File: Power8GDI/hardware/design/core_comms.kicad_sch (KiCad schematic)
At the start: 16 parts, among them U103 TCAN1042HGVDRQ1, U104 TLIN1029ADRQ1

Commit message: Checkpoint integrated 37-sheet schematic before Huge scope revision
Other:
- note added: "CAN1_H/L are vehicle-side nets. STB high by default; MCU PH2 pad43 enables low. DNP termination only after network topology review. EMC/ESD bench qualification pending. CAN2 and LIN2 use the comms2 sheet. PH2/PH3 GPIO additions are provisional schematic assignments."
- note removed: "CAN1_H/L are vehicle-side nets. STB high by default; MCU PH2 pad43 enables low. DNP termination only after network topology review. EMC/ESD bench qualification pending. CAN2 and LIN2 remain unassigned. PH2/PH3 GPIO additions are provisional schematic assignments."
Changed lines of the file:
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@@
 (wire (pts (xy 204.47 123.19) (xy 204.47 130.81)) (stroke (width 0) (type default)))
 (global_label "CAN1_L" (shape bidirectional) (at 204.47 130.81 90) (effects (font (size 1.016 1.016)) (justify right bottom)))
-(text "CAN1_H/L are vehicle-side nets. STB high by default; MCU PH2 pad43 enables low.\nDNP termination only after network topology review. EMC/ESD bench qualification pending.\nCAN2 and LIN2 remain unassigned. PH2/PH3 GPIO additions are provisional schematic assignments." (at 25.4 175 0) (effects (font (size 1.27 1.27)) (justify left top)))
+(text "CAN1_H/L are vehicle-side nets. STB high by default; MCU PH2 pad43 enables low.\nDNP termination only after network topology review. EMC/ESD bench qualification pending.\nCAN2 and LIN2 use the comms2 sheet. PH2/PH3 GPIO additions are provisional schematic assignments." (at 25.4 175 0) (effects (font (size 1.27 1.27)) (justify left top)))
 (symbol (lib_id "Power8GDI_Core:PESD2CAN") (at 245.11 129.54 0) (unit 1) (in_bom yes) (on_board yes) (dnp no) (property "Reference" "D101" (at 245.11 121.92 0) (effects (font (size 1.27 1.27)))) (property "Value" "PESD2CAN" (at 245.11 137.16 0) (effects (font (size 1.27 1.27)))) (property "Footprint" "Package_TO_SOT_SMD:SOT-23" (at 245.11 129.54 0) (effects (font (size 1.27 1.27)) (hide yes))) (property "Design note" "Nexperia Rev2 pinning1/2lines3common; close connector; ground surge return review" (at 245.11 129.54 0) (effects (font (size 1.27 1.27)) (hide yes))) (pin "1") (pin "2") (pin "3") (instances (project "Power8GDI_Core" (path "/f4d21065-0a5b-5086-a08e-1af9469f04bd/a46f09d2-745d-5ec9-9128-e45b02fcfc2a" (reference "D101") (unit 1)))))
 (wire (pts (xy 234.95 124.46) (xy 227.33 124.46)) (stroke (width 0) (type default)))

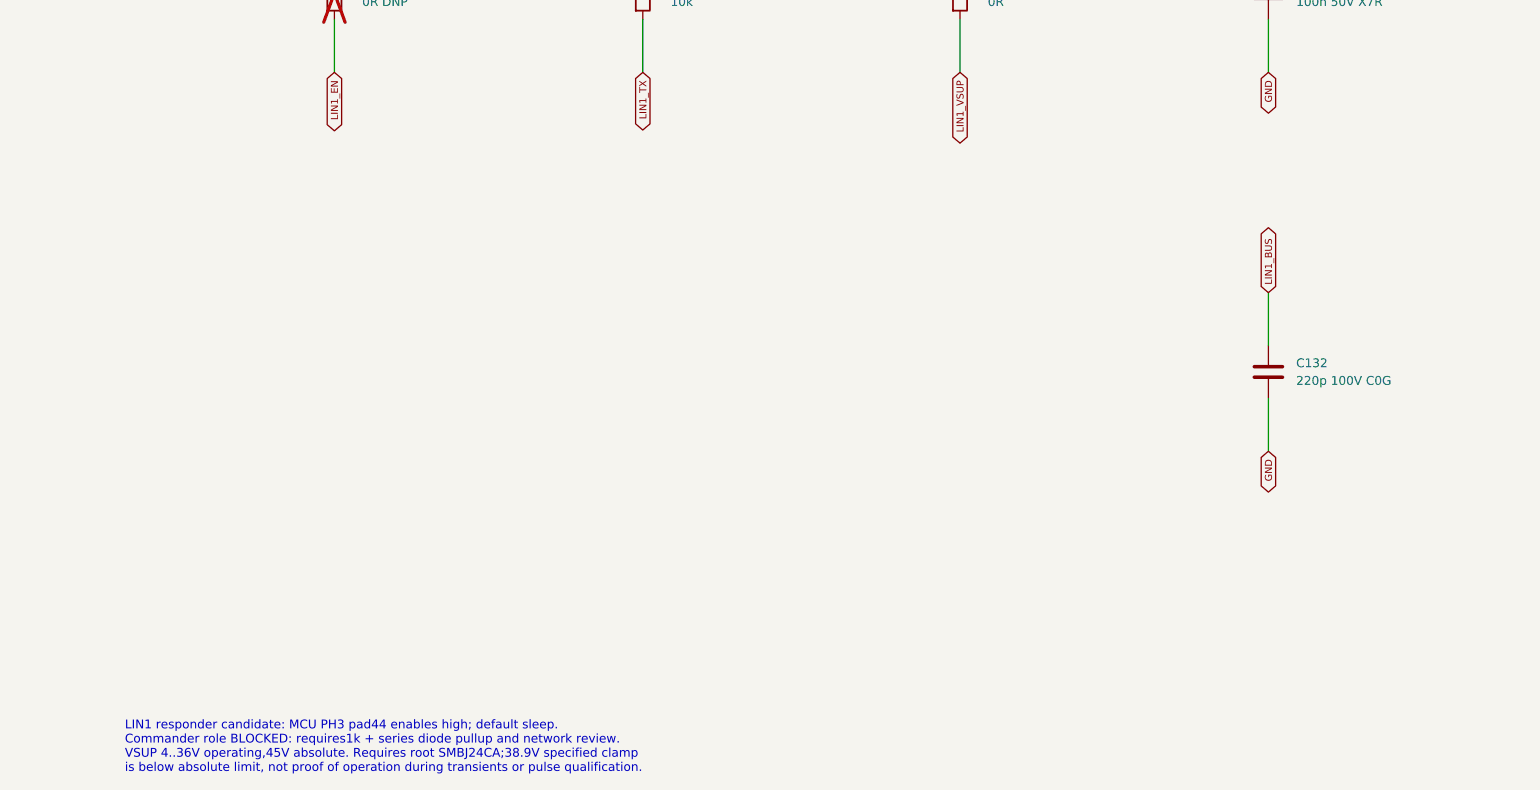
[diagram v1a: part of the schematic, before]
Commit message: Integrate protected GDI and CAN wideband nodes with Huge channel allocation
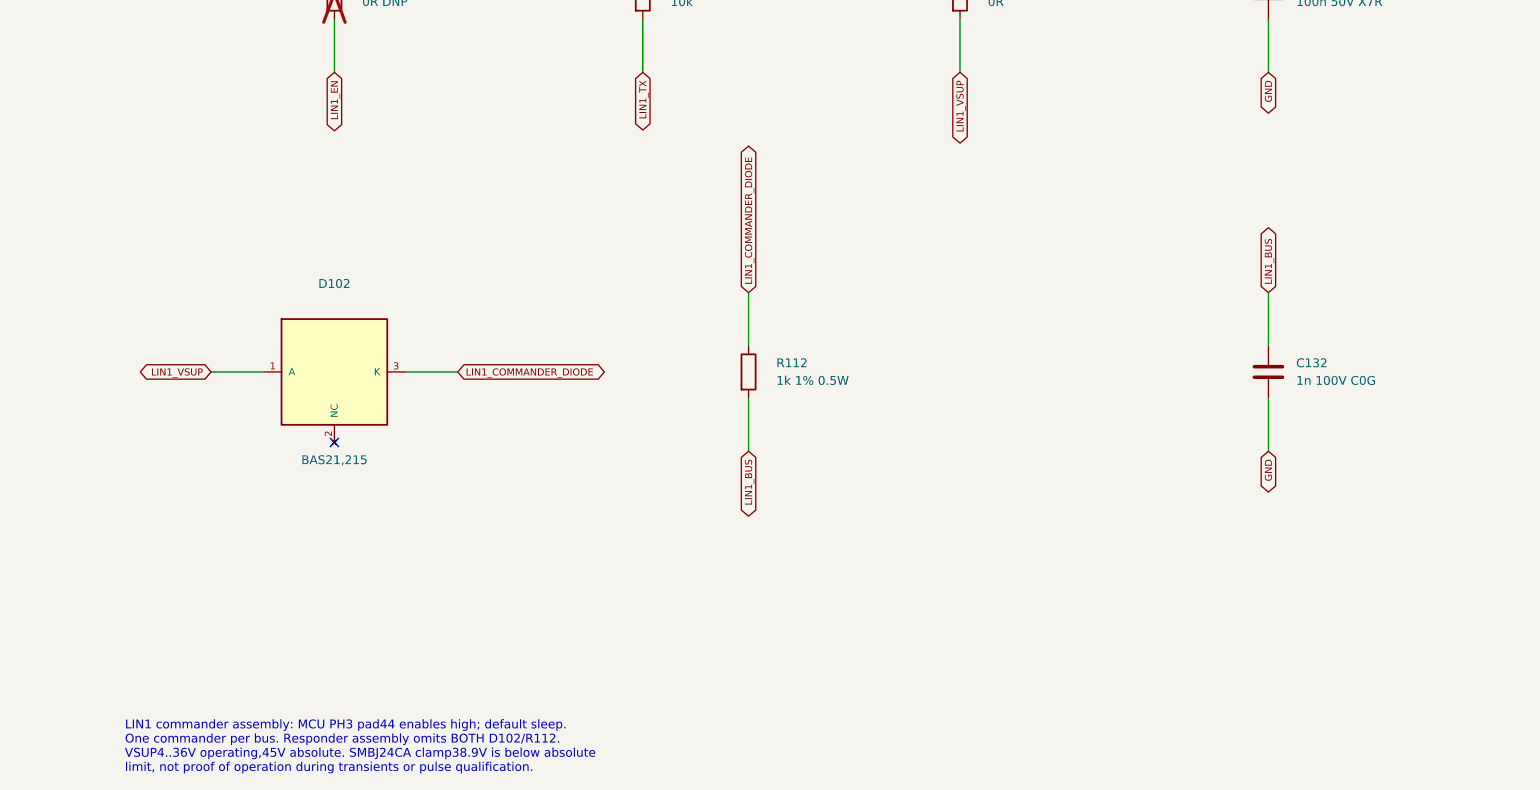
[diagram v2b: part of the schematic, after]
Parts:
- added D102: BAS21,215, Package_TO_SOT_SMD:SOT-23, symbol Power8GDI_Core:Core_BAS21
- added R112: 1k 1% 0.5W, Resistor_SMD:R_1206_3216Metric, symbol Power8GDI_Core:R
- C132: value 220p 100V C0G -> 1n 100V C0G; Design note Respondermode buscap TI Fig10-1; busEMC/loadbudget pending -> Commander bus capacitance; verify total cable/node capacita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
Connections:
- net LIN1_BUS: now also R112.2
- net LIN1_VSUP: now also D102.1 (A)
- new net LIN1_COMMANDER_DIODE: D102.3 (K), R112.1
- no-connect marks 2 -> 3
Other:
- note added: "LIN1 commander assembly: MCU PH3 pad44 enables high; default sleep. One commander per bus. Responder assembly omits BOTH D102/R112. VSUP4..36V operating,45V absolute. SMBJ24CA clamp38.9V is below absolute limit, not proof of operation during transients or pulse qualification."
- note removed: "LIN1 responder candidate: MCU PH3 pad44 enables high; default sleep. Commander role BLOCKED: requires1k + series diode pullup and network review. VSUP 4..36V operating,45V absolute. Requires root SMBJ24CA;38.9V specified clamp is below absolute limit, not proof of operation during transients or pulse qualification."
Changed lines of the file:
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@@
 (wire (pts (xy 510.54 168.91) (xy 510.54 176.53)) (stroke (width 0) (type default)))
 (global_label "GND" (shape bidirectional) (at 510.54 176.53 90) (effects (font (size 1.016 1.016)) (justify right bottom)))
-(symbol (lib_id "Power8GDI_Core:C") (at 464.82 219.71 0) (unit 1) (in_bom yes) (on_board yes) (dnp no) (property "Reference" "C132" (at 468.82 218.44 0) (effects (font (size 1.27 1.27)) (justify left))) (property "Value" "220p 100V C0G" (at 468.82 220.98 0) (effects (font (size 1.27 1.27)) (justify left))) (property "Footprint" "Capacitor_SMD:C_0603_1608Metric" (at 464.82 219.71 0) (effects (font (size 1.27 1.27)) (hide yes))) (property "Design note" "Respondermode buscap TI Fig10-1; busEMC/loadbudget pending" (at 464.82 219.71 0) (effects (font (size 1.27 1.27)) (hide yes))) (pin "1") (pin "2") (instances (project "Power8GDI_Core" (path "/f4d21065-0a5b-5086-a08e-1af9469f04bd/a46f09d2-745d-5ec9-9128-e45b02fcfc2a" (reference "C132") (unit 1)))))
+(symbol (lib_id "Power8GDI_Core:C") (at 464.82 219.71 0) (unit 1) (in_bom yes) (on_board yes) (dnp no) (property "Reference" "C132" (at 468.82 218.44 0) (effects (font (size 1.27 1.27)) (justify left))) (property "Value" "1n 100V C0G" (at 468.82 220.98 0) (effects (font (size 1.27 1.27)) (justify left))) (property "Footprint" "Capacitor_SMD:C_0603_1608Metric" (at 464.82 219.71 0) (effects (font (size 1.27 1.27)) (hide yes))) (property "Design note" "Commander bus capacitance; verify total cable/node capacitance" (at 464.82 219.71 0) (effects (font (size 1.27 1.27)) (hide yes))) (pin "1") (pin "2") (instances (project "Power8GDI_Core" (path "/f4d21065-0a5b-5086-a08e-1af9469f04bd/a46f09d2-745d-5ec9-9128-e45b02fcfc2a" (reference "C132") (unit 1)))))
 (wire (pts (xy 464.82 215.9) (xy 464.82 208.28)) (stroke (width 0) (type default)))
 (global_label "LIN1_BUS" (shape bidirectional) (at 464.82 208.28 270) (effects (font (size 1.016 1.016)) (justify left bottom)))
 (wire (pts (xy 464.82 223.52) (xy 464.82 231.14)) (stroke (width 0) (type default)))
 (global_label "GND" (shape bidirectional) (at 464.82 231.14 90) (effects (font (size 1.016 1.016)) (justify right bottom)))
-(text "LIN1 responder candidate: MCU PH3 pad44 enables high; default sleep.\nCommander role BLOCKED: requires1k + series diode pullup and network review.\nVSUP 4..36V operating,45V absolute. Requires root SMBJ24CA;38.9V specified clamp\nis below absolute limit, not proof of operation during transients or pulse qualification." (at 300 270 0) (effects (font (size 1.27 1.27)) (justify left top)))
+(symbol (lib_id "Power8GDI_Core:Core_BAS21") (at 330.2 219.71 0) (unit 1) (in_bom yes) (on_board yes) (dnp no) (property "Reference" "D102" (at 330.2 207.01 0) (effects (font (size 1.27 1.27)))) (property "Value" "BAS21,215" (at 330.2 232.41 0) (effects (font (size 1.27 1.27)))) (property "Footprint" "Package_TO_SOT_SMD:SOT-23" (at 330.2 219.71 0) (effects (font (size 1.27 1.27)) (hide yes))) (property "Design note" "Commander assembly; remove D102 and R112 for responder-only topology" (at 330.2 219.71 0) (effects (font (size 1.27 1.27)) (hide yes))) (pin "1") (pin "3") (pin "2") (instances (project "Power8GDI_Core" (path "/f4d21065-0a5b-5086-a08e-1af9469f04bd/a46f09d2-745d-5ec9-9128-e45b02fcfc2a" (reference "D102") (unit 1)))))
+(wire (pts (xy 320.04 219.71) (xy 312.42 219.71)) (stroke (width 0) (type default)))
+(global_label "LIN1_VSUP" (shape bidirectional) (at 312.42 219.71 0) (effects (font (size 1.016 1.016)) (justify right bottom)))
+(wire (pts (xy 340.36 219.71) (xy 347.98 219.71)) (stroke (width 0) (type default)))
+(global_label "LIN1_COMMANDER_DIODE" (shape bidirectional) (at 347.98 219.71 180) (effects (font (size 1.016 1.016)) (justify left bottom)))
+(no_connect (at 330.2 229.87))
+(symbol (lib_id "Power8GDI_Core:R") (at 389.89 219.71 0) (unit 1) (in_bom yes) (on_board yes) (dnp no) (property "Reference" "R112" (at 393.89 218.44 0) (effects (font (size 1.27 1.27)) (justify left))) (property "Value" "1k 1% 0.5W" (at 393.89 220.98 0) (effects (font (size 1.27 1.27)) (justify left))) (property "Footprint" "Resistor_SMD:R_1206_3216Metric" (at 389.89 219.71 0) (effects (font (size 1.27 1.27)) (hide yes))) (property "Design note" "16V dominant bound0.256W; pulse/voltage derating must be checked" (at 389.89 219.71 0) (effects (font (size 1.27 1.27)) (hide yes))) (pin "1") (pin "2") (instances (project "Power8GDI_Core" (path "/f4d21065-0a5b-5086-a08e-1af9469f04bd/a46f09d2-745d-5ec9-9128-e45b02fcfc2a" (reference "R112") (unit 1)))))
+(wire (pts (xy 389.89 215.9) (xy 389.89 208.28)) (stroke (width 0) (type default)))
+(global_label "LIN1_COMMANDER_DIODE" (shape bidirectional) (at 389.89 208.28 270) (effects (font (size 1.016 1.016)) (justify left bottom)))
+(wire (pts (xy 389.89 223.52) (xy 389.89 231.14)) (stroke (width 0) (type default)))
+(global_label "LIN1_BUS" (shape bidirectional) (at 389.89 231.14 90) (effects (font (size 1.016 1.016)) (justify right bottom)))
+(text "LIN1 commander assembly: MCU PH3 pad44 enables high; default sleep.\nOne commander per bus. Responder assembly omits BOTH D102/R112.\nVSUP4..36V operating,45V absolute. SMBJ24CA clamp38.9V is below absolute\nlimit, not proof of operation during transients or pulse qualification." (at 300 270 0) (effects (font (size 1.27 1.27)) (justify left top)))
 (sheet_instances (path "/" (page "1"))))

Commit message: Review B58 injector power stage and bind selected GDI6 BOM
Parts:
- C127, C128, C130: Hardware_Qualification (none) -> BOARD_QUALIFICATION_PENDING; MPN (none) -> C0603C104K5RACTU; Manufacturer (none) -> KEMET; Procurement_Status (none) -> SELECTED_CATALOG_ITEM; Purchase_Released (none) -> false; Selection_Gaps (none) -> []; Selection_ID (none) -> SEL-6bf9727c4e40; Selection_Ratings (none) -> {"capacitance_pf": 100000, "dielectric": "X7R", "rated_volt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; Selection_Source_URLs (none) -> https://search.kemet.com/download/specsheet/C0603C104K5RACTU
- C131: Hardware_Qualification (none) -> BOARD_QUALIFICATION_PENDING; MPN (none) -> C0805C105K5RACTU; Manufacturer (none) -> KEMET; Procurement_Status (none) -> SELECTED_CATALOG_ITEM; Purchase_Released (none) -> false; Selection_Gaps (none) -> []; Selection_ID (none) -> SEL-838906dbfe60; Selection_Ratings (none) -> {"capacitance_pf": 1000000, "dc_bias_qualification": "PENDI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; Selection_Source_URLs (none) -> https://search.kemet.com/component-documentation/download/s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
- C132: Hardware_Qualification (none) -> BOARD_QUALIFICATION_PENDING; MPN (none) -> C0603C102J1GACTU; Manufacturer (none) -> KEMET; Procurement_Status (none) -> SELECTED_CATALOG_ITEM; Purchase_Released (none) -> false; Selection_Gaps (none) -> []; Selection_ID (none) -> SEL-ec742f39ec1f; Selection_Ratings (none) -> {"capacitance_pf": 1000, "dielectric": "C0G", "rated_voltag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; Selection_Source_URLs (none) -> https://search.kemet.com/download/specsheet/C0603C102J1GACTU
- D101: Hardware_Qualification (none) -> PINOUT_RATINGS_AND_DELIVERY_SUFFIX_REVIEW_PENDING; MPN (none) -> PESD2CAN,215; Manufacturer (none) -> Nexperia; Procurement_Status (none) -> REFERENCE_MPN_RETAINED; Purchase_Released (none) -> false; Selection_Gaps (none) -> ["Existing schematic MPN retained. Complete circuit rating/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; Selection_ID (none) -> SEL-397878b612f9; Selection_Ratings (none) -> {}; Selection_Source_URLs (none) -> https://www.nexperia.com/product/PESD2CAN
- D102: Hardware_Qualification (none) -> PINOUT_RATINGS_AND_DELIVERY_SUFFIX_REVIEW_PENDING; MPN (none) -> BAS21,215; Manufacturer (none) -> Nexperia; Procurement_Status (none) -> REFERENCE_MPN_RETAINED; Purchase_Released (none) -> false; Selection_Gaps (none) -> ["Existing schematic MPN retained. Complete circuit rating/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; Selection_ID (none) -> SEL-3ac3f96db10b; Selection_Ratings (none) -> {}; Selection_Source_URLs (none) -> https://www.nexperia.com/product/BAS21
- R104, R108, R110: Hardware_Qualification (none) -> BOARD_QUALIFICATION_PENDING; MPN (none) -> CRCW060310K0FKEA; Manufacturer (none) -> Vishay; Procurement_Status (none) -> SELECTED_FAMILY_CODE; Purchase_Released (none) -> false; Selection_Gaps (none) -> []; Selection_ID (none) -> SEL-9c0806476875; Selection_Ratings (none) -> {"aec_q200": true, "derating": "Use manufacturer power vers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; Selection_Source_URLs (none) -> https://www.vishay.com/docs/20035/dcrcwe3.pdf
- R107: Hardware_Qualification (none) -> BOARD_QUALIFICATION_PENDING; MPN (none) -> CRCW06034K70FKEA; Manufacturer (none) -> Vishay; Procurement_Status (none) -> SELECTED_FAMILY_CODE; Purchase_Released (none) -> false; Selection_Gaps (none) -> []; Selection_ID (none) -> SEL-1f010ac9622d; Selection_Ratings (none) -> {"aec_q200": true, "derating": "Use manufacturer power vers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; Selection_Source_URLs (none) -> https://www.vishay.com/docs/20035/dcrcwe3.pdf
- R111: Hardware_Qualification (none) -> BOARD_QUALIFICATION_PENDING; MPN (none) -> CRCW06030000Z0EA; Manufacturer (none) -> Vishay; Procurement_Status (none) -> SELECTED_FAMILY_CODE; Purchase_Released (none) -> false; Selection_Gaps (none) -> []; Selection_ID (none) -> SEL-8473f02313b2; Selection_Ratings (none) -> {"aec_q200": true, "current_a": 2, "power_reference_tempera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; Selection_Source_URLs (none) -> https://www.vishay.com/docs/20035/dcrcwe3.pdf
- R112: Hardware_Qualification (none) -> BOARD_QUALIFICATION_PENDING; MPN (none) -> CRCW12061K00FKEAHP; Manufacturer (none) -> Vishay; Procurement_Status (none) -> SELECTED_CATALOG_ITEM; Purchase_Released (none) -> false; Selection_Gaps (none) -> []; Selection_ID (none) -> SEL-515f600e0ec3; Selection_Ratings (none) -> {"aec_q200": true, "derating": "Use manufacturer power vers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; Selection_Source_URLs (none) -> https://www.vishay.com/docs/20043/crcwhpe3.pdf https://www.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
- U103: Hardware_Qualification (none) -> PINOUT_RATINGS_AND_DELIVERY_SUFFIX_REVIEW_PENDING; MPN (none) -> TCAN1042HGVDRQ1; Manufacturer (none) -> Texas Instruments; Procurement_Status (none) -> REFERENCE_MPN_RETAINED; Purchase_Released (none) -> false; Selection_Gaps (none) -> ["Existing schematic MPN retained. Complete circuit rating/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; Selection_ID (none) -> SEL-c86778911c36; Selection_Ratings (none) -> {}; Selection_Source_URLs (none) -> https://www.ti.com/product/TCAN1042H-Q1/part-details/TCAN10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
- U104: Hardware_Qualification (none) -> PINOUT_RATINGS_AND_DELIVERY_SUFFIX_REVIEW_PENDING; MPN (none) -> TLIN1029ADRQ1; Manufacturer (none) -> Texas Instruments; Procurement_Status (none) -> REFERENCE_MPN_RETAINED; Purchase_Released (none) -> false; Selection_Gaps (none) -> ["Existing schematic MPN retained. Complete circuit rating/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; Selection_ID (none) -> SEL-d38cf124d61a; Selection_Ratings (none) -> {}; Selection_Source_URLs (none) -> https://www.ti.com/product/TLIN1029A-Q1/part-details/TLIN10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
